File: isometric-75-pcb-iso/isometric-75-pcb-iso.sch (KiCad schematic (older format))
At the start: 25 parts, among them Q101 AO3400A, SW101 RST, SW102 BOOT, U101 XC6206P332MR, U102 STM32F072CBTx

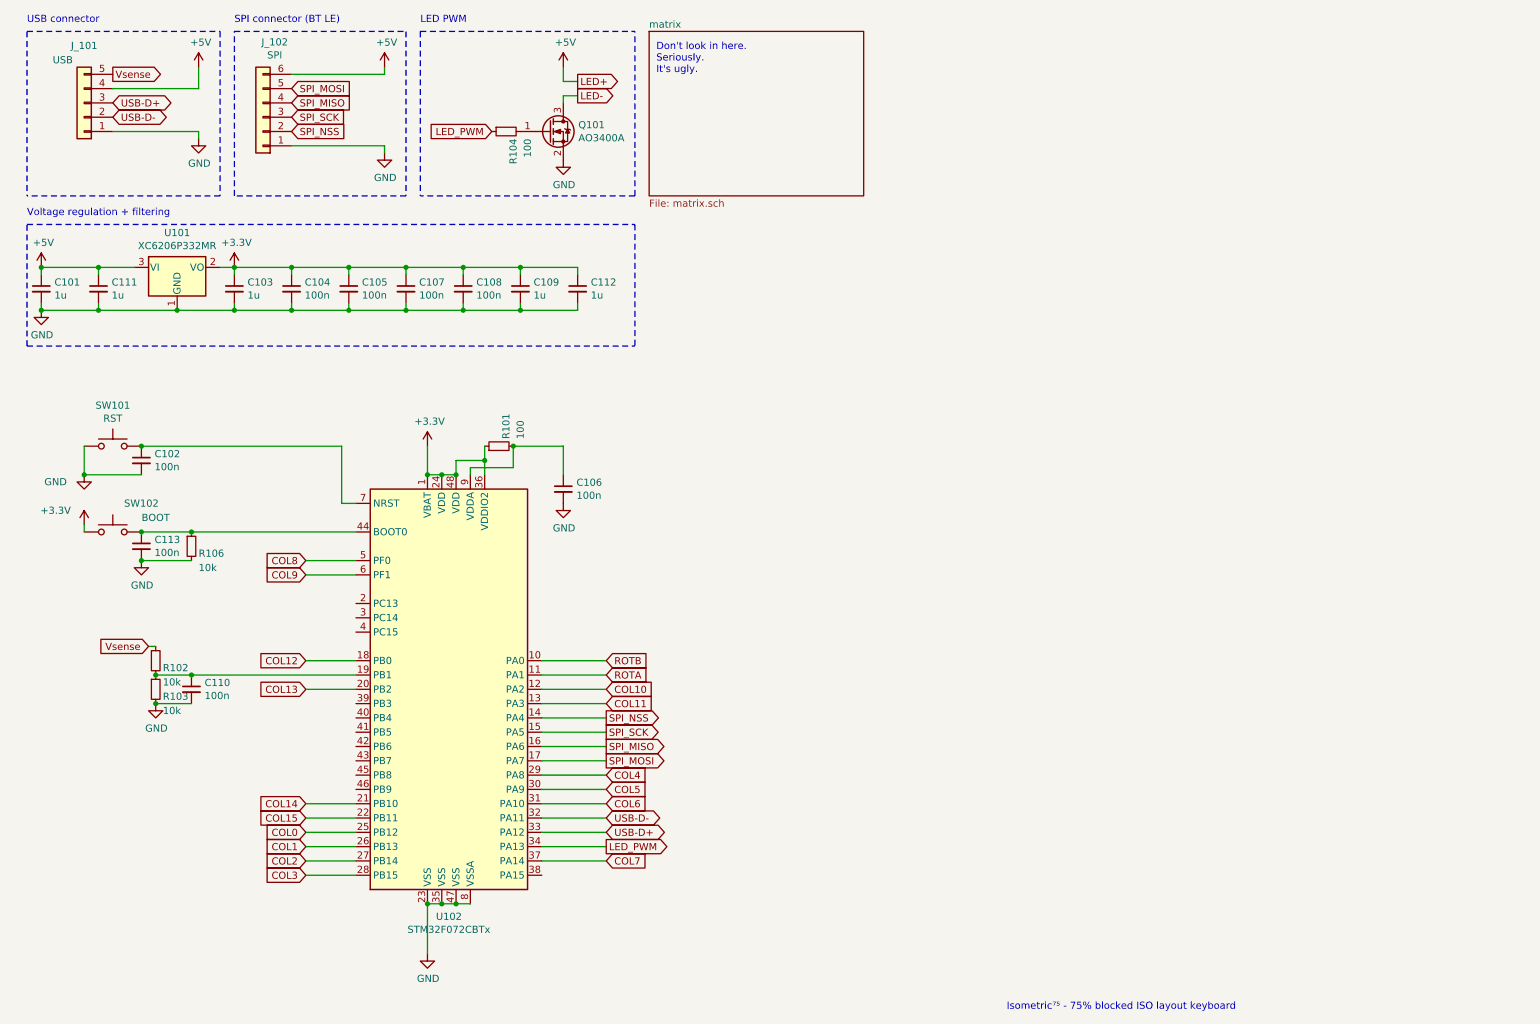
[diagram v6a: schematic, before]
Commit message: added underglow
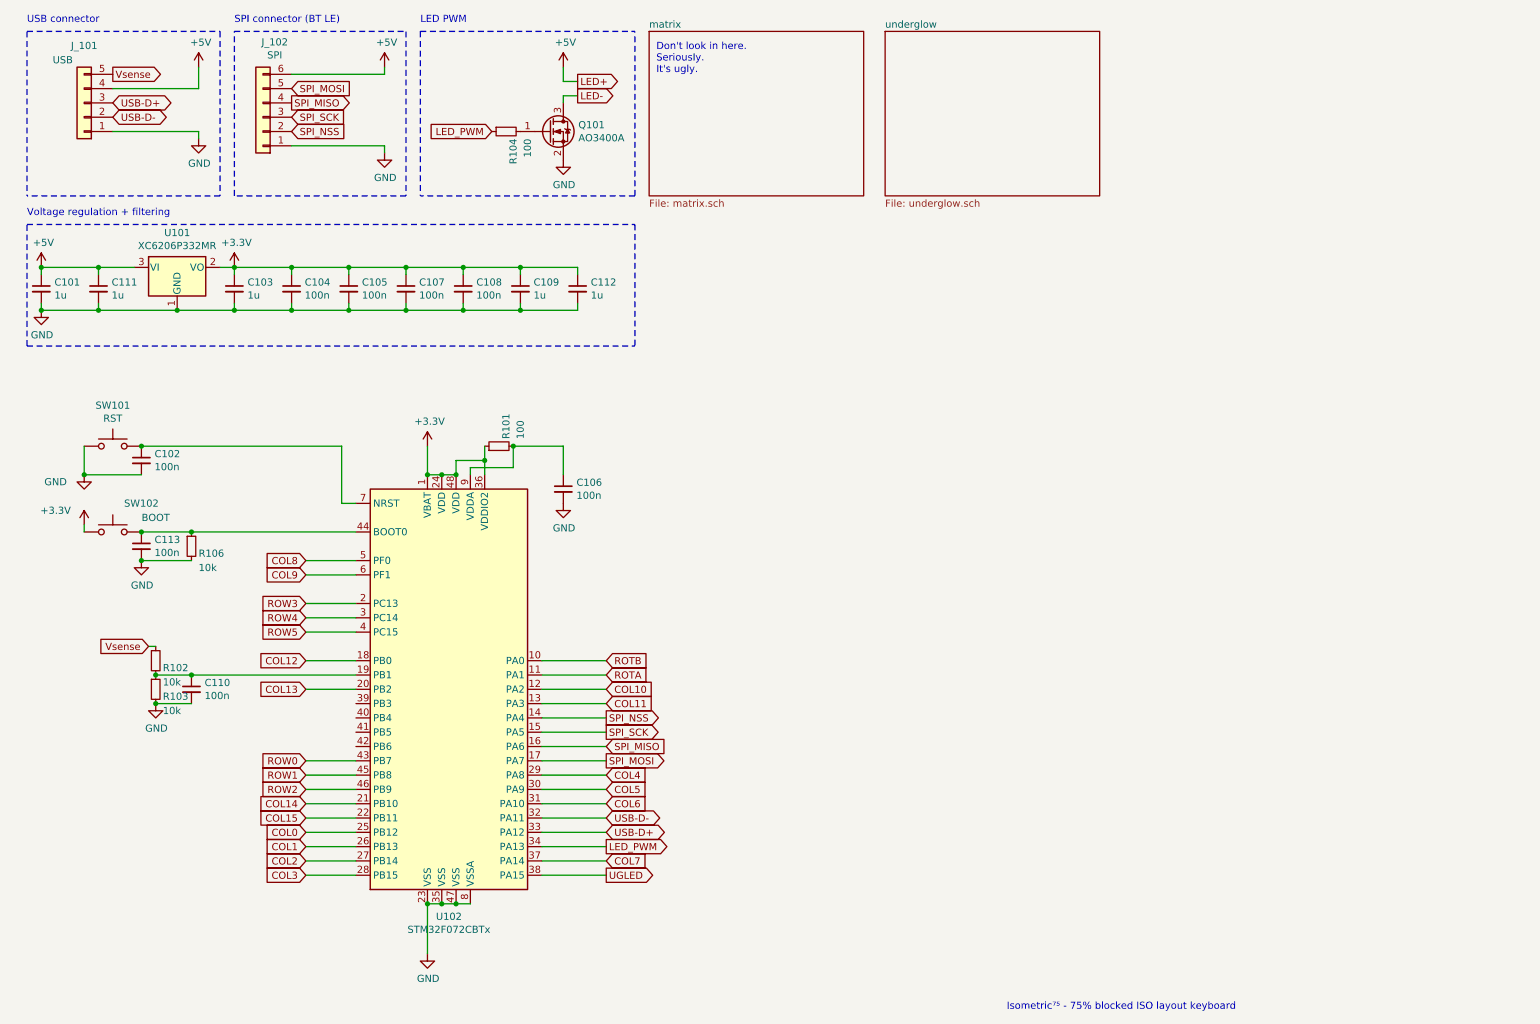
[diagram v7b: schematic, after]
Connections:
- net ROW3: now reaches U102.2 (PC13)
- net ROW4: now reaches U102.3 (PC14)
- net UGLED: now reaches U102.38 (PA15)
- net ROW5: now reaches U102.4 (PC15)
- net ROW0: now reaches U102.43 (PB7)
- net ROW1: now reaches U102.45 (PB8)
- net ROW2: now reaches U102.46 (PB9)
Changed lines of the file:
@@
 $Descr A4 11693 8268
 encoding utf-8
-Sheet 1 2
+Sheet 1 3
 Title ""
 Date ""
@@
 Text GLabel 4600 5550 2    50   Output ~ 0
 SPI_SCK
-Text GLabel 4600 5650 2    50   Output ~ 0
+Text GLabel 4600 5650 2    50   Input ~ 0
 SPI_MISO
 Text GLabel 4600 5750 2    50   Output ~ 0
@@
 Text GLabel 2400 1250 2    50   Input ~ 0
 SPI_SCK
-Text GLabel 2400 1150 2    50   Input ~ 0
+Text GLabel 2400 1150 2    50   Output ~ 0
 SPI_MISO
 Text GLabel 2400 1050 2    50   Input ~ 0
@@
 	-1   0    0    1
 $EndComp
+Text GLabel 2500 4850 0    50   Input ~ 0
+ROW5
+Text GLabel 2500 4750 0    50   Input ~ 0
+ROW4
+Text GLabel 2500 4650 0    50   Input ~ 0
+ROW3
+Wire Wire Line
+	2500 4850 2850 4850
+Wire Wire Line
+	2500 4750 2850 4750
+Wire Wire Line
+	2500 4650 2850 4650
+Text GLabel 2500 5950 0    50   Input ~ 0
+ROW2
+Text GLabel 2500 5850 0    50   Input ~ 0
+ROW1
+Text GLabel 2500 5750 0    50   Input ~ 0
+ROW0
+Wire Wire Line
+	2500 5750 2850 5750
+Wire Wire Line
+	2500 5850 2850 5850
+Wire Wire Line
+	2500 5950 2850 5950
+$Sheet
+S 6550 650  1500 1150
+U 5E6E13F7
+F0 "underglow" 50
+F1 "underglow.sch" 50
+$EndSheet
+Text GLabel 4600 6550 2    50   Output ~ 0
+UGLED
+Wire Wire Line
+	4600 6550 4150 6550
 $EndSCHEMATC

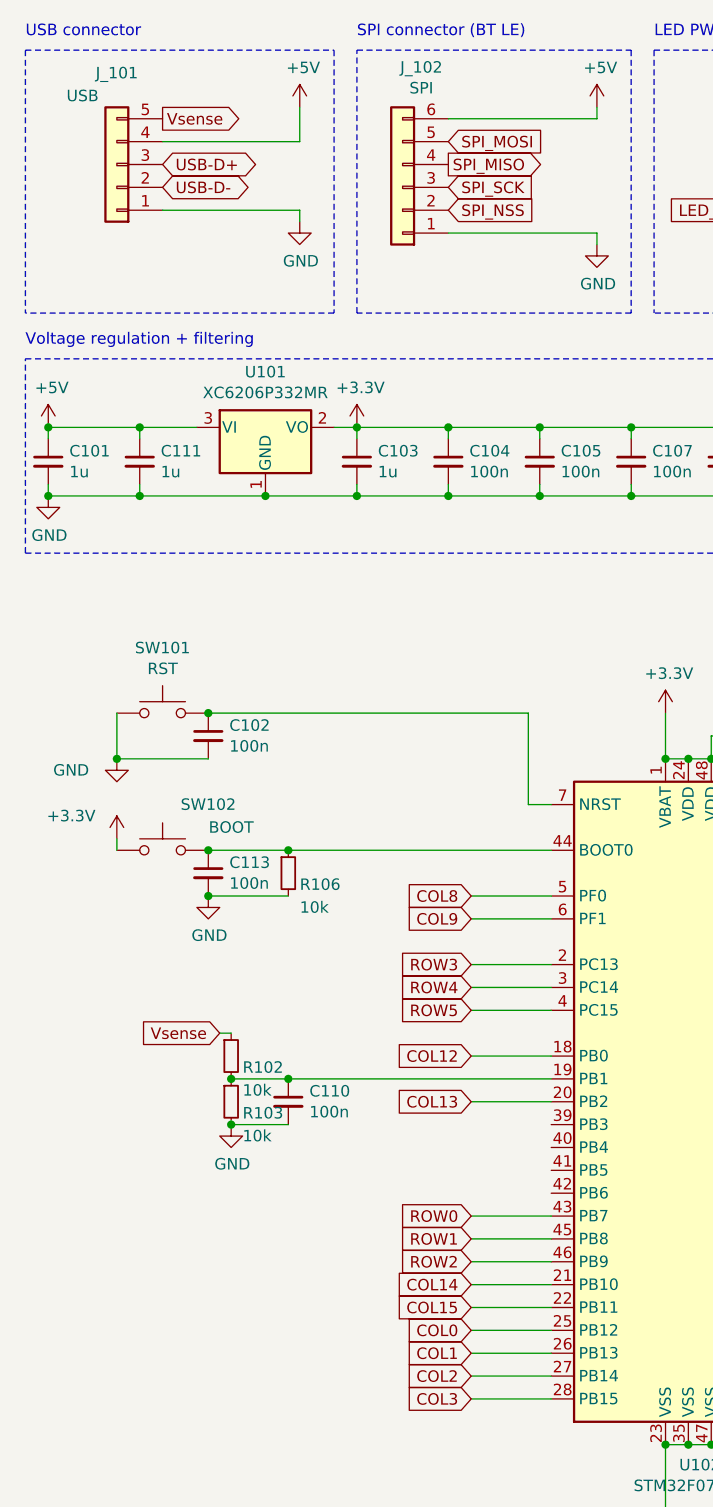
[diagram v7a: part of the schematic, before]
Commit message: added ground planes, various minor fixes
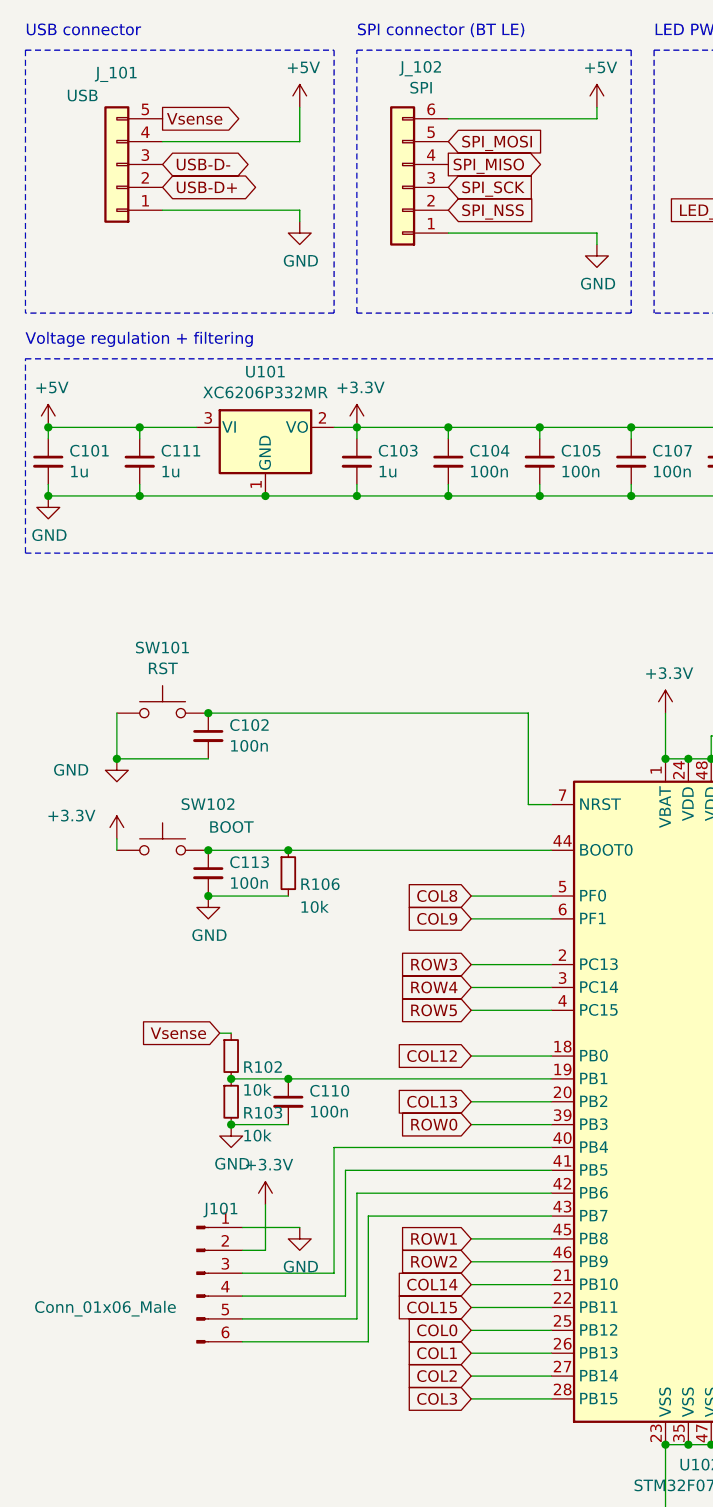
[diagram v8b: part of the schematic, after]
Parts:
- added J101: Conn_01x06_Male, Connector_PinHeader_2.54mm:PinHeader_1x06_P2.54mm_Vertical, symbol Connector:Conn_01x06_Male
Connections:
- net +3V3: now also J101.2 (Pin_2)
- net GND: now also J101.1 (Pin_1)
- net ROW0: now also U102.39 (PB3); no longer U102.43 (PB7)
- net USB-D+: now also J_101.2 (Pin_2); no longer J_101.3 (Pin_3)
- net USB-D-: now also J_101.3 (Pin_3); no longer J_101.2 (Pin_2)
- net at U102.40 (PB4): now also J101.3 (Pin_3)
- net at U102.41 (PB5): now also J101.4 (Pin_4)
- net at U102.42 (PB6): now also J101.5 (Pin_5)
- new net: J101.6 (Pin_6), U102.43 (PB7)
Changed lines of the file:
@@
 Text GLabel 1150 950  2    50   Output ~ 0
 Vsense
+Text GLabel 1150 1250 2    50   BiDi ~ 0
+USB-D+
 Text GLabel 1150 1150 2    50   BiDi ~ 0
-USB-D+
-Text GLabel 1150 1250 2    50   BiDi ~ 0
 USB-D-
 $Comp
@@
 Text GLabel 2500 5850 0    50   Input ~ 0
 ROW1
-Text GLabel 2500 5750 0    50   Input ~ 0
+Text GLabel 2500 5350 0    50   Input ~ 0
 ROW0
-Wire Wire Line
-	2500 5750 2850 5750
 Wire Wire Line
 	2500 5850 2850 5850
@@
 Wire Wire Line
 	4600 6550 4150 6550
+Wire Wire Line
+	2500 5350 2850 5350
+$Comp
+L Connector:Conn_01x06_Male J101
+U 1 1 5EB0D7C5
+P 1300 6000
+F 0 "J101" H 1408 6281 50  0000 C CNN
+F 1 "Conn_01x06_Male" H 900 5850 50  0000 C CNN
+F 2 "Connector_PinHeader_2.54mm:PinHeader_1x06_P2.54mm_Vertical" H 1300 6000 50  0001 C CNN
+F 3 "~" H 1300 6000 50  0001 C CNN
+	1    1300 6000
+	1    0    0    -1
+$EndComp
+Wire Wire Line
+	2050 5750 2050 6300
+Wire Wire Line
+	2050 6300 1500 6300
+Wire Wire Line
+	2050 5750 2850 5750
+Wire Wire Line
+	1500 6200 2000 6200
+Wire Wire Line
+	2000 6200 2000 5650
+Wire Wire Line
+	2000 5650 2850 5650
+Wire Wire Line
+	1950 5550 1950 6100
+Wire Wire Line
+	1950 6100 1500 6100
+Wire Wire Line
+	1950 5550 2850 5550
+Wire Wire Line
+	1500 6000 1900 6000
+Wire Wire Line
+	1900 6000 1900 5450
+Wire Wire Line
+	1900 5450 2850 5450
+$Comp
+L power:GND #PWR0120
+U 1 1 5EB39B3C
+P 1750 5800
+F 0 "#PWR0120" H 1750 5550 50  0001 C CNN
+F 1 "GND" H 1755 5627 50  0000 C CNN
+F 2 "" H 1750 5800 50  0001 C CNN
+F 3 "" H 1750 5800 50  0001 C CNN
+	1    1750 5800
+	1    0    0    -1
+$EndComp
+Wire Wire Line
+	1600 5900 1500 5900
+Wire Wire Line
+	1500 5800 1750 5800
+Wire Wire Line
+	1600 5700 1600 5900
+$Comp
+L power:+3.3V #PWR?
+U 1 1 5EB54C29
+P 1600 5700
+F 0 "#PWR?" H 1600 5550 50  0001 C CNN
+F 1 "+3.3V" H 1615 5873 50  0000 C CNN
+F 2 "" H 1600 5700 50  0001 C CNN
+F 3 "" H 1600 5700 50  0001 C CNN
+	1    1600 5700
+	1    0    0    -1
+$EndComp
 $EndSCHEMATC
